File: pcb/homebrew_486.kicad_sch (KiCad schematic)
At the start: 4 parts

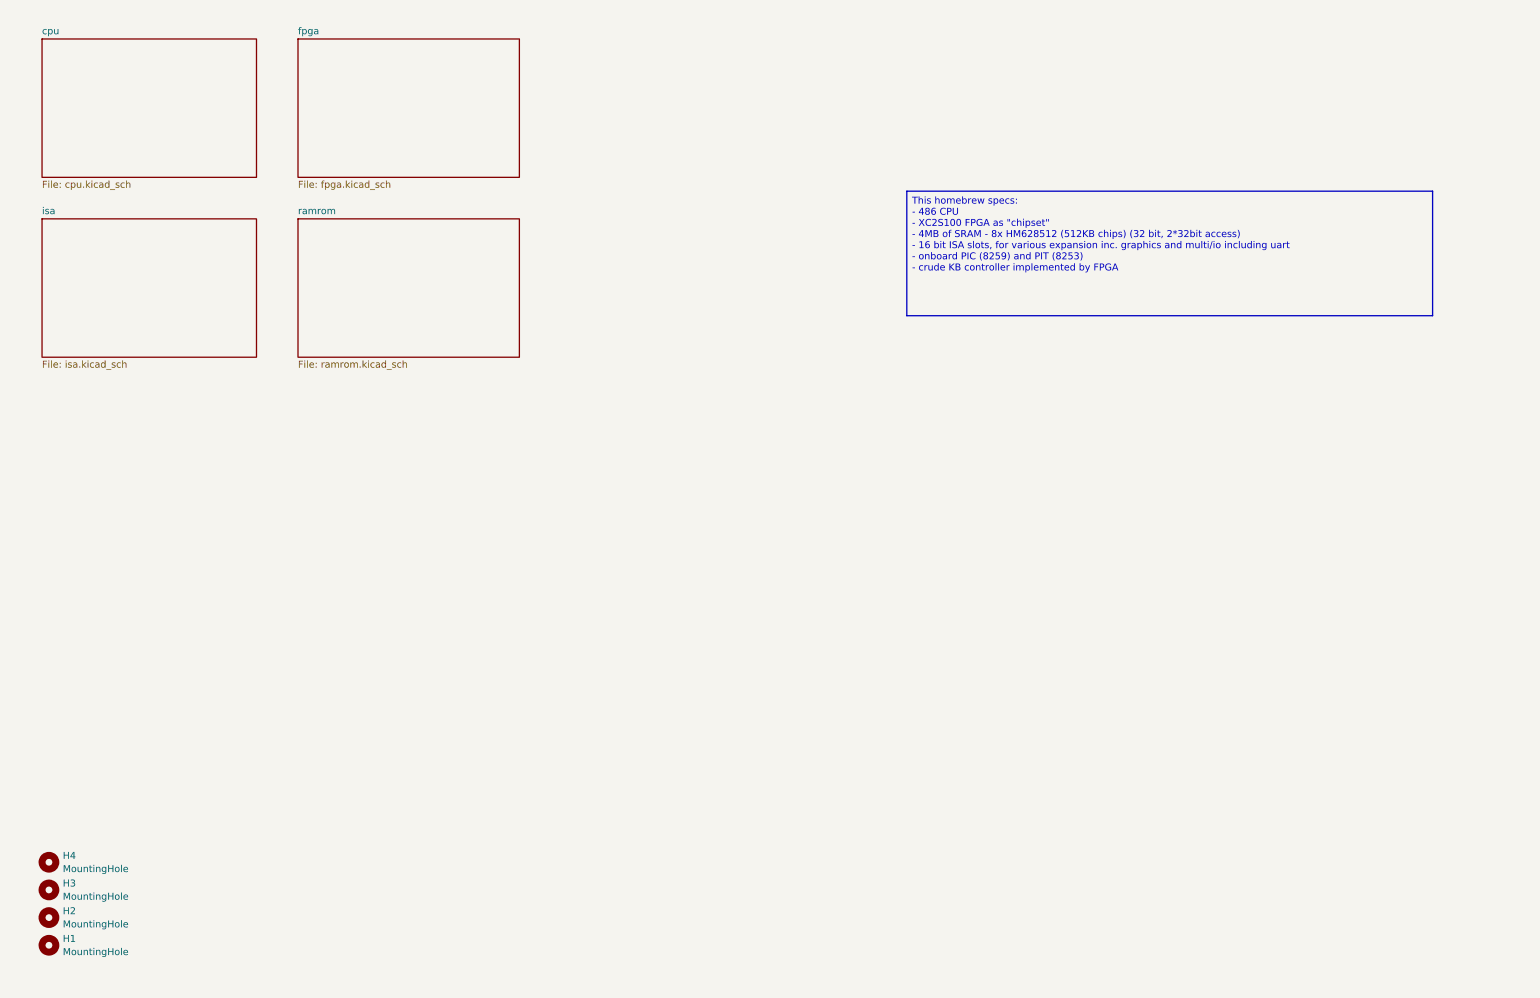
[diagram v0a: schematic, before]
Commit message: Add fpga sources, update schematic, update README
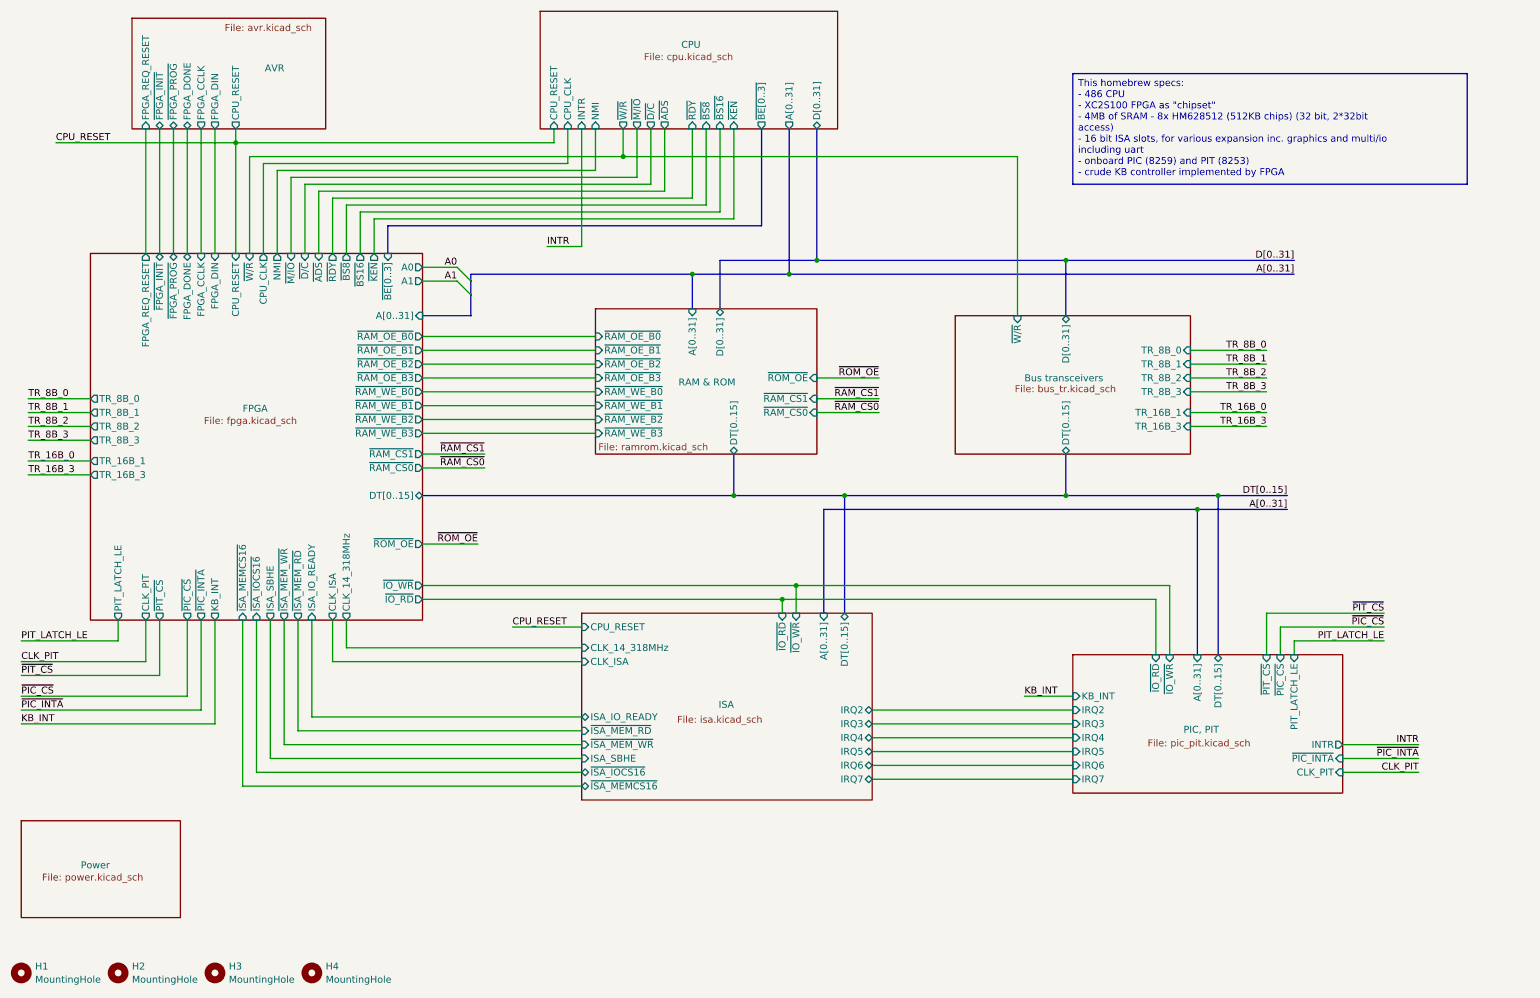
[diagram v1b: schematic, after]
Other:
- sheet cpu renamed CPU
- sheet fpga renamed FPGA
- sheet isa renamed ISA
- sheet ramrom renamed RAM & ROM
- added sheet AVR (avr.kicad_sch)
- added sheet Bus transceivers (bus_tr.kicad_sch)
- added sheet PIC, PIT (pic_pit.kicad_sch)
- added sheet Power (power.kicad_sch)
- sheet CPU ports: added A[0..31], CPU_CLK, CPU_RESET, D[0..31], INTR, NMI, ~{ADS}, ~{BE[0..3]}, ~{BS16}, ~{BS8}, ~{D/C}, ~{KEN}, ~{M/IO}, ~{RDY}, ~{W/R}; removed none
- sheet FPGA ports: added A0, A1, A[0..31], CLK_14_318MHz, CLK_ISA, CLK_PIT, CPU_CLK, CPU_RESET, DT[0..15], FPGA_CCLK, FPGA_DIN, FPGA_DONE, FPGA_REQ_RESET, ISA_IO_READY, ISA_SBHE, KB_INT, NMI, PIT_LATCH_LE, TR_16B_1, TR_16B_3, TR_8B_0, TR_8B_1, TR_8B_2, TR_8B_3, ~{ADS}, ~{BE[0..3]}, ~{BS16}, ~{BS8}, ~{D/C}, ~{FPGA_INIT}, ~{FPGA_PROG}, ~{IO_RD}, ~{IO_WR}, ~{ISA_IOCS16}, ~{ISA_MEMCS16}, ~{ISA_MEM_RD}, ~{ISA_MEM_WR}, ~{KEN}, ~{M/IO}, ~{PIC_CS}, ~{PIC_INTA}, ~{PIT_CS}, ~{RAM_CS0}, ~{RAM_CS1}, ~{RAM_OE_B0}, ~{RAM_OE_B1}, ~{RAM_OE_B2}, ~{RAM_OE_B3}, ~{RAM_WE_B0}, ~{RAM_WE_B1}, ~{RAM_WE_B2}, ~{RAM_WE_B3}, ~{RDY}, ~{ROM_OE}, ~{W/R}; removed none
- sheet ISA ports: added A[0..31], CLK_14_318MHz, CLK_ISA, CPU_RESET, DT[0..15], IRQ2, IRQ3, IRQ4, IRQ5, IRQ6, IRQ7, ISA_IO_READY, ISA_SBHE, ~{IO_RD}, ~{IO_WR}, ~{ISA_IOCS16}, ~{ISA_MEMCS16}, ~{ISA_MEM_RD}, ~{ISA_MEM_WR}; removed none
- sheet RAM & ROM ports: added A[0..31], DT[0..15], D[0..31], ~{RAM_CS0}, ~{RAM_CS1}, ~{RAM_OE_B0}, ~{RAM_OE_B1}, ~{RAM_OE_B2}, ~{RAM_OE_B3}, ~{RAM_WE_B0}, ~{RAM_WE_B1}, ~{RAM_WE_B2}, ~{RAM_WE_B3}, ~{ROM_OE}; removed none
- moved on the sheet: H1, H2, H3, H4

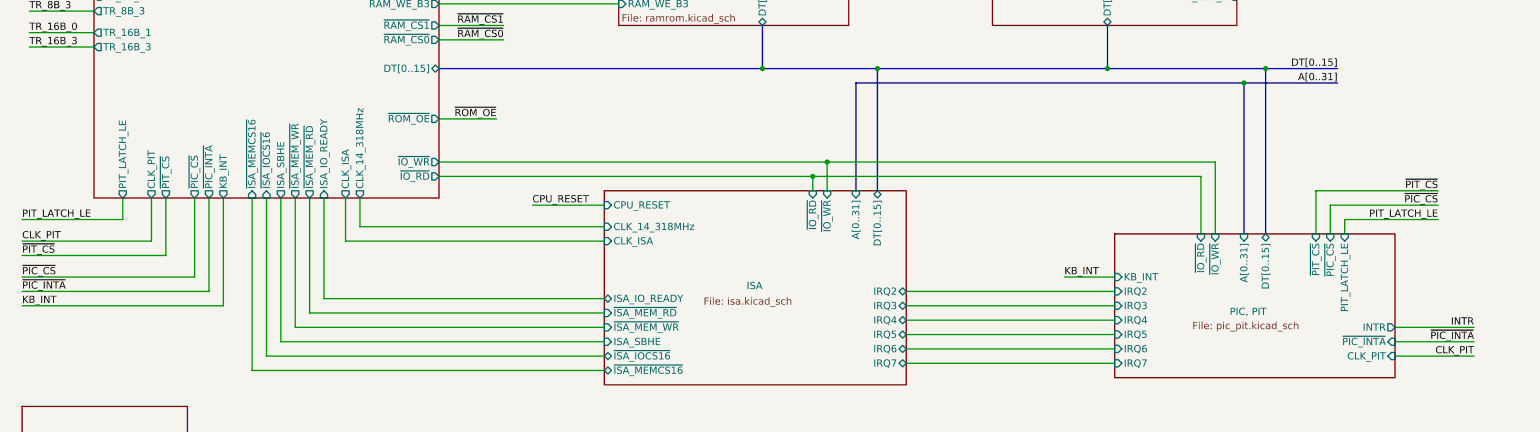
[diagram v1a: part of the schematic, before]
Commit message: updating diagram and pcb to removed U23, driving PIT gate2 directly by PIT_SPK_GATE (former PIT_LATCH_LE), 635 VIAs
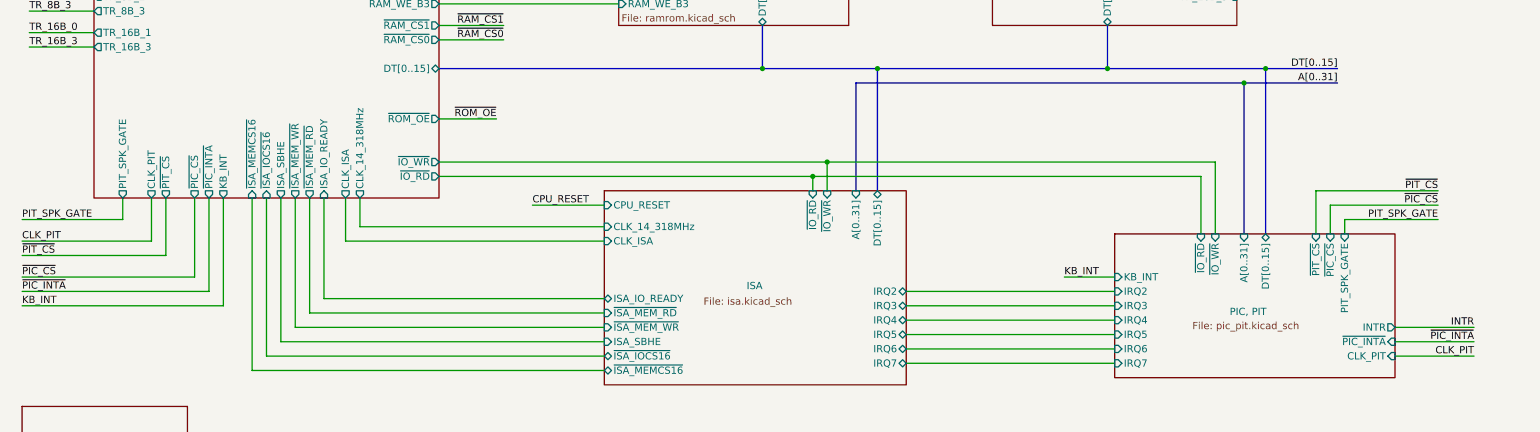
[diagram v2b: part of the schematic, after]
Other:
- sheet FPGA ports: added PIT_SPK_GATE; removed PIT_LATCH_LE
- sheet PIC, PIT ports: added PIT_SPK_GATE; removed PIT_LATCH_LE
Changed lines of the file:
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@@
 		)
 	)
-	(label "PIT_LATCH_LE"
+	(label "PIT_SPK_GATE"
 		(at 266.7 132.08 180)
 		(effects
@@
 		)
 	)
-	(label "PIT_LATCH_LE"
+	(label "PIT_SPK_GATE"
 		(at 16.51 132.08 0)
 		(effects
@@
 			)
 		)
-		(pin "PIT_LATCH_LE" output
+		(pin "PIT_SPK_GATE" output
 			(at 34.29 128.27 270)
 			(effects
@@
 			)
 		)
-		(pin "PIT_LATCH_LE" input
+		(pin "PIT_SPK_GATE" input
 			(at 250.19 134.62 90)
 			(effects

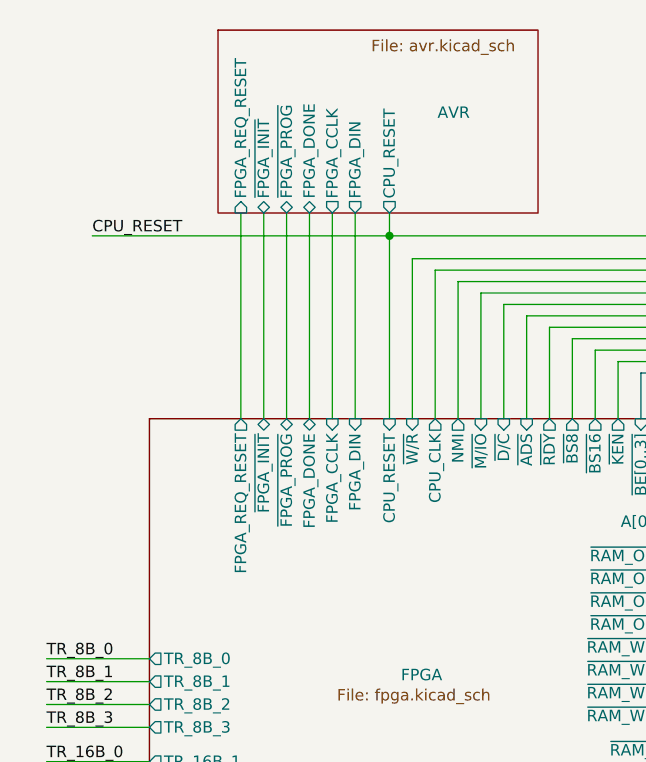
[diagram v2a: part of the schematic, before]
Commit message: removing redundant global labels
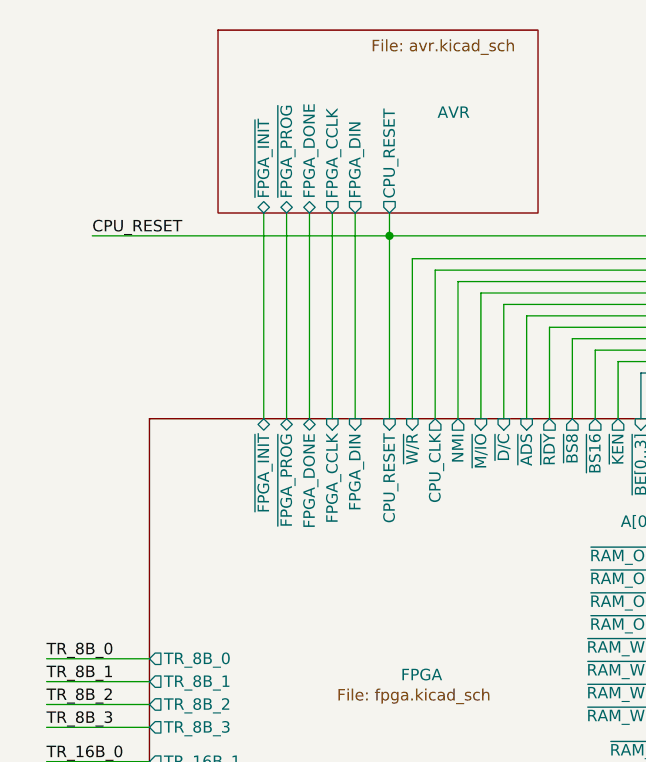
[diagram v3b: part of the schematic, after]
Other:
- sheet AVR ports: added none; removed FPGA_REQ_RESET
- sheet FPGA ports: added none; removed FPGA_REQ_RESET
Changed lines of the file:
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@@
-		)
-	)
-	(wire
-		(pts
-			(xy 39.37 38.1) (xy 39.37 60.96)
-		)
-		(stroke
-			(width 0)
-			(type default)
 		)
 	)
@@
 			)
 		)
-		(pin "FPGA_REQ_RESET" input
-			(at 39.37 38.1 270)
-			(effects
-				(font
-					(size 1.27 1.27)
-				)
-				(justify left)
-			)
-		)
 		(pin "~{FPGA_PROG}" bidirectional
 			(at 44.45 38.1 270)
@@
 			(effects
 				(font
-					(size 1.27 1.27)
-				)
-				(justify right)
-			)
-		)
-		(pin "FPGA_REQ_RESET" output
-			(at 39.37 60.96 90)
-			(effects
-				(font

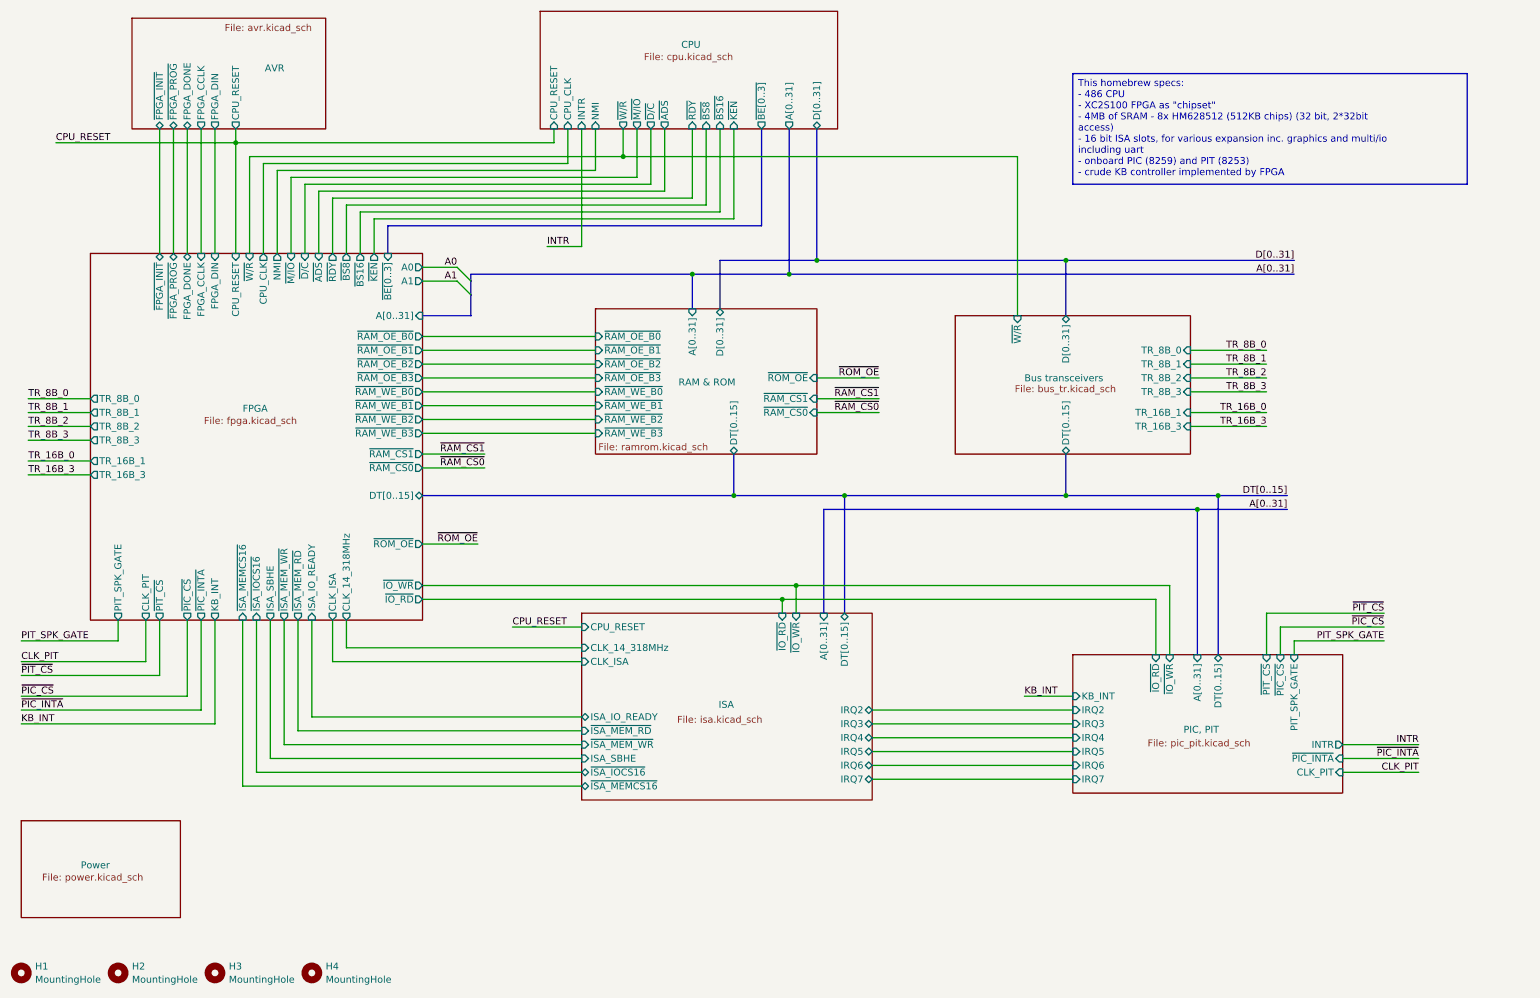
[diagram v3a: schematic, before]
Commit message: added Address Bus buffers. Dummy NetTies for now, to be replaced with 74AHCT541
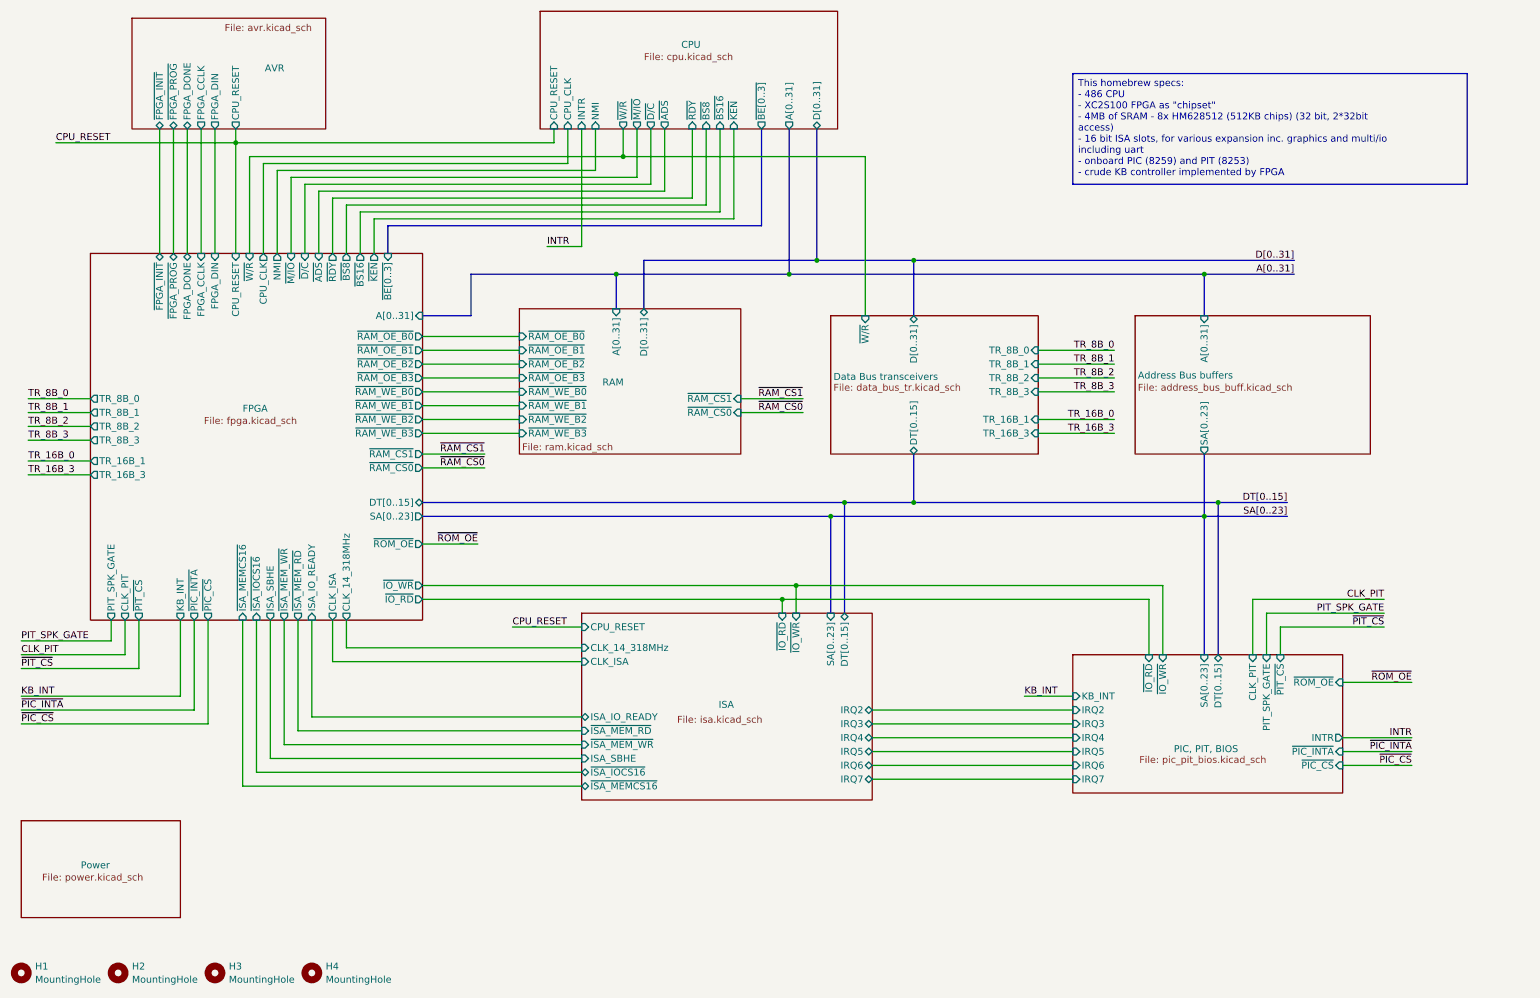
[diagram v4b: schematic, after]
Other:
- sheet Bus transceivers renamed Data Bus transceivers
- sheet PIC, PIT renamed PIC, PIT, BIOS
- sheet RAM & ROM renamed RAM
- added sheet Address Bus buffers (address_bus_buff.kicad_sch)
- sheet Data Bus transceivers: file bus_tr.kicad_sch -> data_bus_tr.kicad_sch
- sheet FPGA ports: added SA[0..23]; removed A0, A1
- sheet ISA ports: added SA[0..23]; removed A[0..31]
- sheet PIC, PIT, BIOS: file pic_pit.kicad_sch -> pic_pit_bios.kicad_sch
- sheet PIC, PIT, BIOS ports: added SA[0..23], ~{ROM_OE}; removed A[0..31]
- sheet RAM: file ramrom.kicad_sch -> ram.kicad_sch
- sheet RAM ports: added none; removed DT[0..15], ~{ROM_OE}
